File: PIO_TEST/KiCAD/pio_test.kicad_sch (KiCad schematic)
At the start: 3 parts, among them J1 I/O Port, SW1 SW_DIP_x08

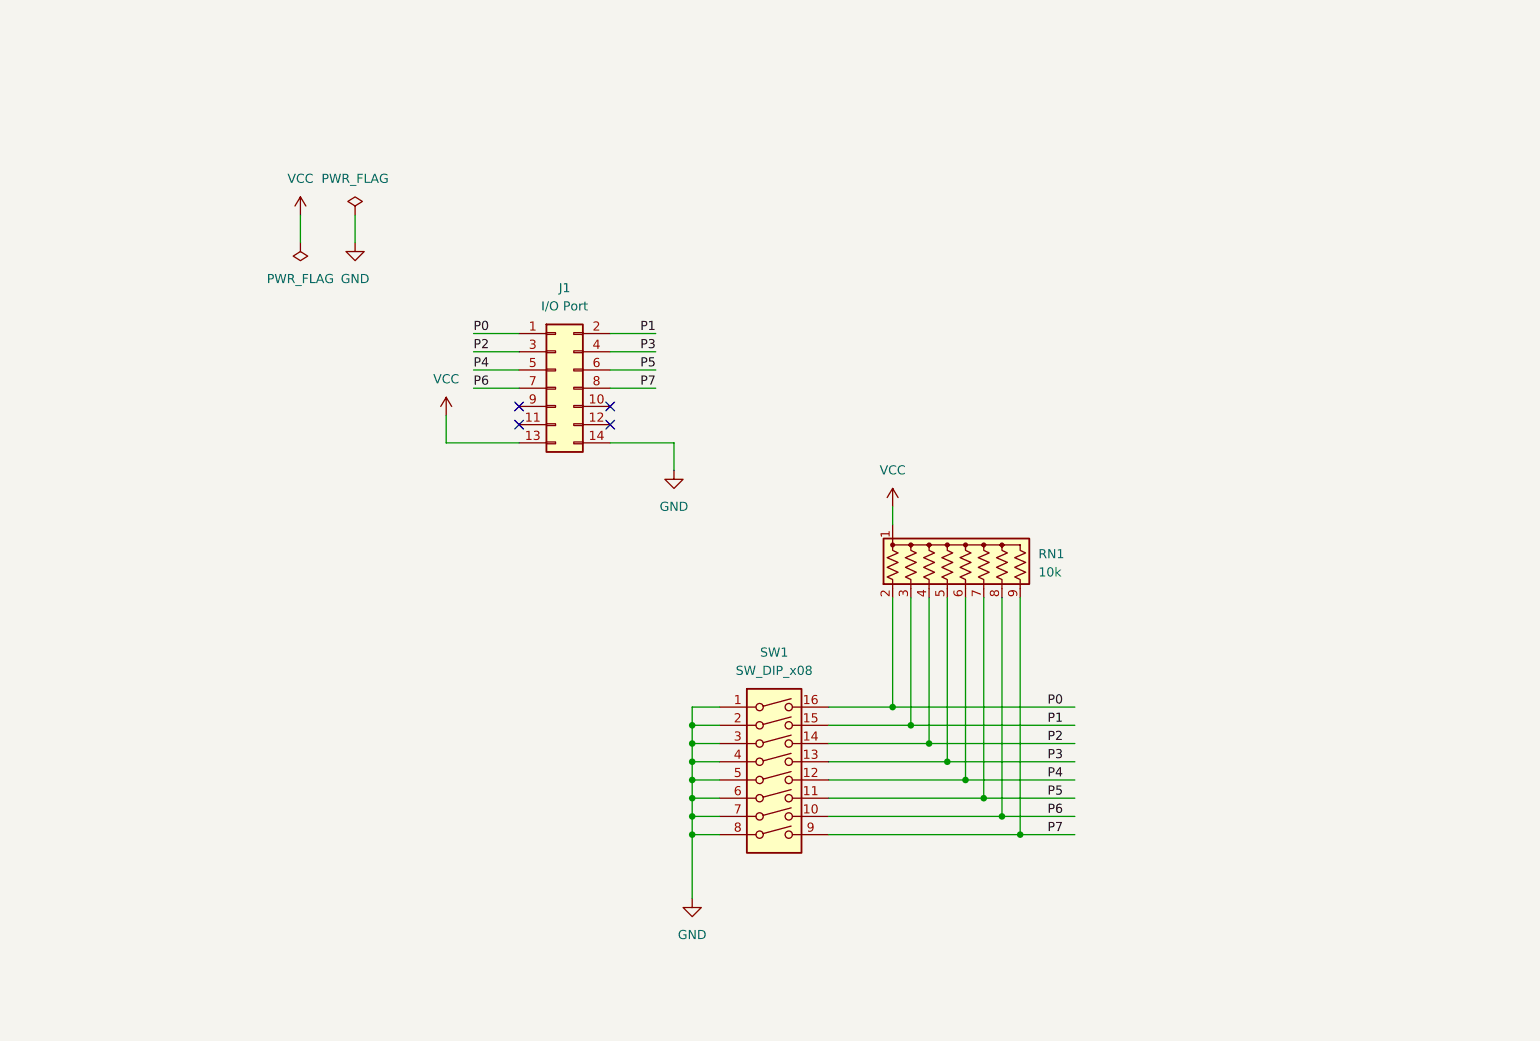
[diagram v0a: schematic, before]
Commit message: PIO 入力基板回路改良
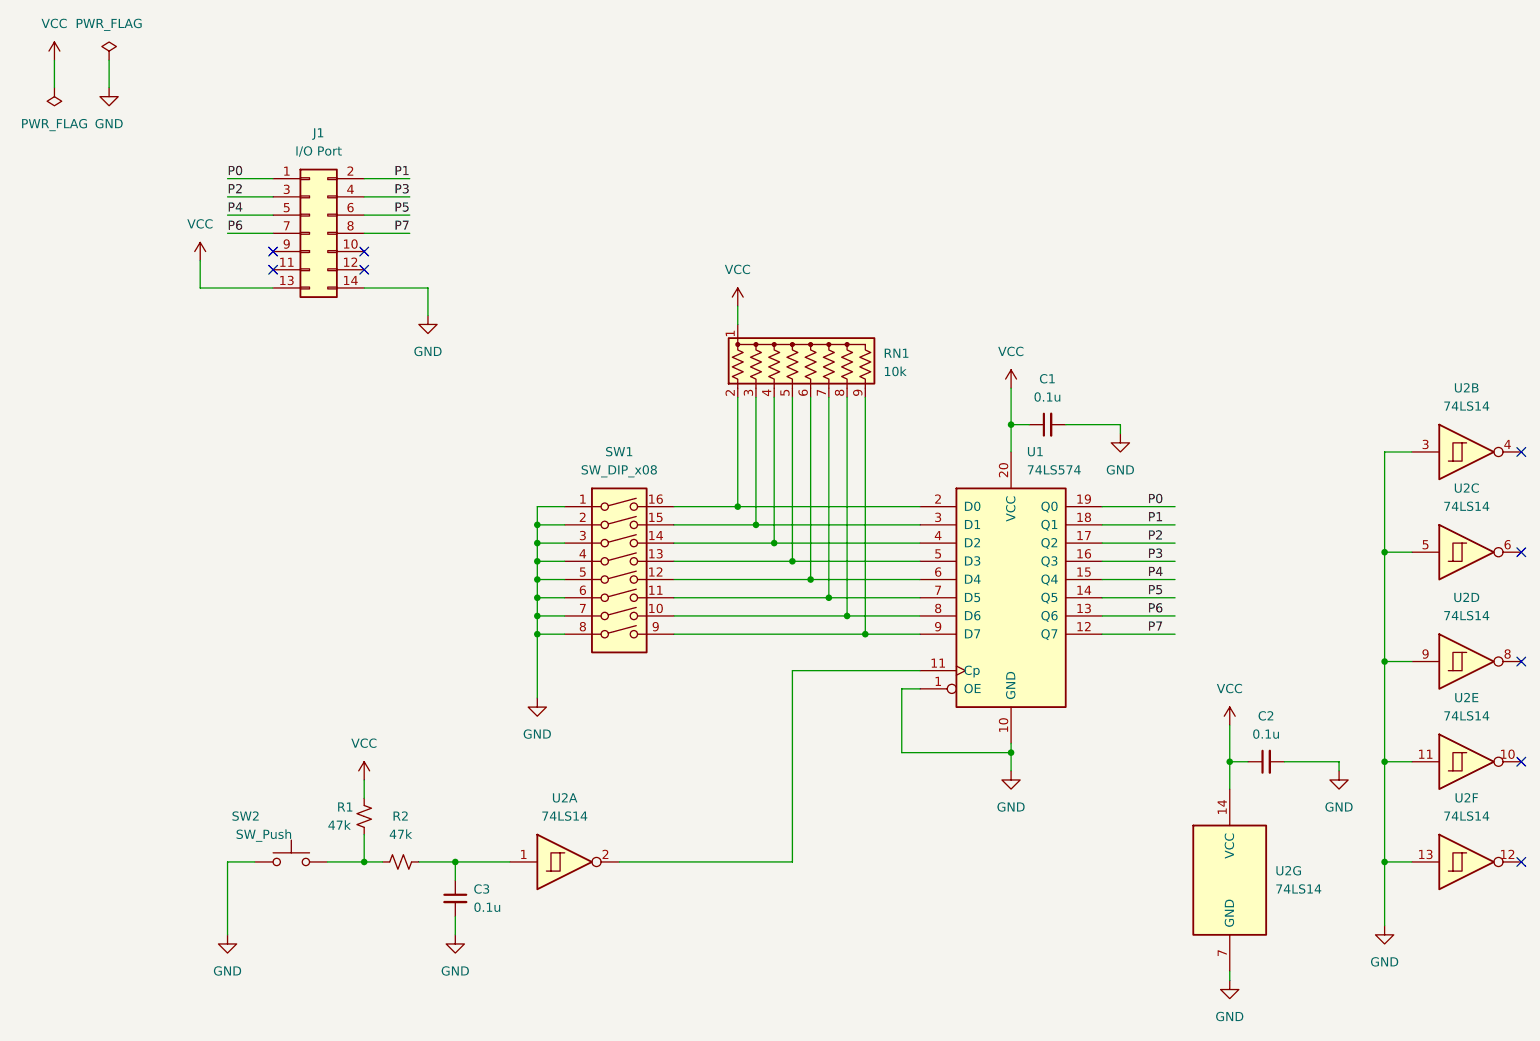
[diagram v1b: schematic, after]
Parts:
- added C1, C2, C3: 0.1u, symbol Device:C_Small
- added R1, R2: 47k, symbol Device:R_Small_US
- added SW2: SW_Push, symbol Switch:SW_Push
- added U1: 74LS574, symbol 74xx:74LS574
- added U2: 74LS14, symbol 74xx:74LS14
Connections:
- net GND: now also C1.2, C2.2, C3.2, SW2.1, U1.1 (OE), U1.10 (GND), U2.11, U2.13, U2.3, U2.5, U2.7 (GND), U2.9
- net P0: now also U1.19 (Q0); no longer RN1.2 (R1), SW1.16
- net P1: now also U1.18 (Q1); no longer RN1.3 (R2), SW1.15
- net P2: now also U1.17 (Q2); no longer RN1.4 (R3), SW1.14
- net P3: now also U1.16 (Q3); no longer RN1.5 (R4), SW1.13
- net P4: now also U1.15 (Q4); no longer RN1.6 (R5), SW1.12
- net P5: now also U1.14 (Q5); no longer RN1.7 (R6), SW1.11
- net P6: now also U1.13 (Q6); no longer RN1.8 (R7), SW1.10
- net P7: now also U1.12 (Q7); no longer RN1.9 (R8), SW1.9
- net VCC: now also C1.1, C2.1, R1.1, U1.20 (VCC), U2.14 (VCC)
- new net: U1.11 (Cp), U2.2
- new net: RN1.2 (R1), SW1.16, U1.2 (D0)
- new net: RN1.3 (R2), SW1.15, U1.3 (D1)
- new net: RN1.4 (R3), SW1.14, U1.4 (D2)
- new net: RN1.5 (R4), SW1.13, U1.5 (D3)
- new net: RN1.6 (R5), SW1.12, U1.6 (D4)
- new net: RN1.7 (R6), SW1.11, U1.7 (D5)
- new net: RN1.8 (R7), SW1.10, U1.8 (D6)
- new net: RN1.9 (R8), SW1.9, U1.9 (D7)
- new net: R1.2, R2.1, SW2.2
- new net: C3.1, R2.2, U2.1
- no-connect marks 4 -> 9
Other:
- moved on the sheet: J1, RN1, SW1
